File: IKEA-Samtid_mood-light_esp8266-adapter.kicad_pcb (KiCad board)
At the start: 2 copper layers, 17.5 x 17.8 mm, 11 parts, among them P1 ESP8266-01, P2 mood-light, U1 AMS1117-3.3

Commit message: ESP8266 adapter: added a bit of copper pour as heatsink.
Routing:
- net +3.3V: track 28.9 -> 31.1 mm
- added copper zone on B.Cu, net +3.3V
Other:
- board text added: "2015 - V0.30.e"
- board text removed: "2015 - V0.30.d"

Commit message: ESP8266 adapter: tweaks.
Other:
- board text added: "p.↑↓R"
- board text removed: "pull↑↓R"

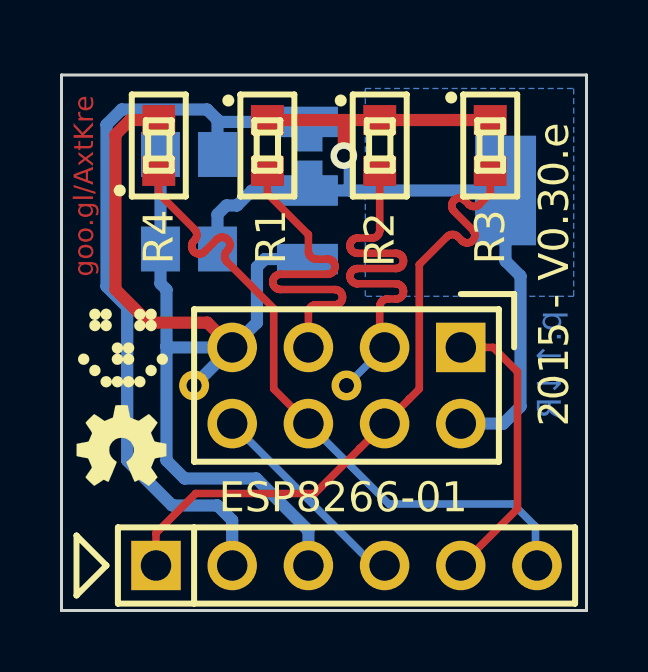
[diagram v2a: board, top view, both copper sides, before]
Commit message: ESP8266 adapter: tweaks.
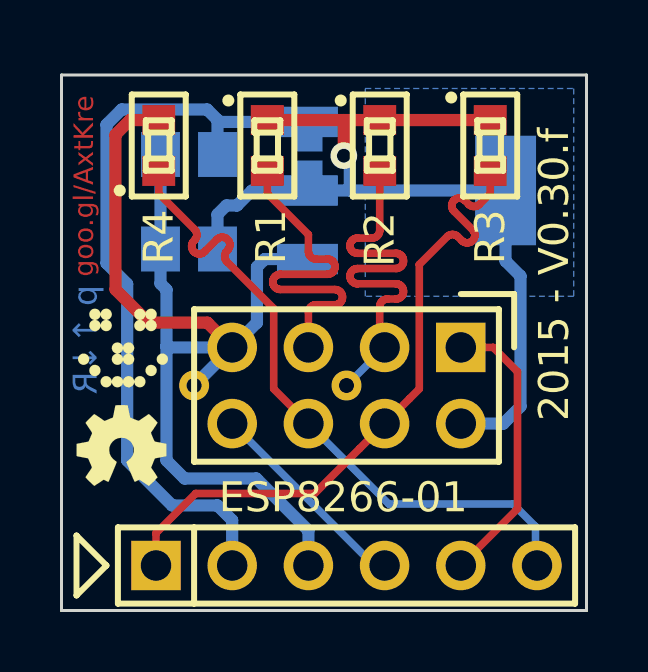
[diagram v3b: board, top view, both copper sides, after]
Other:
- board text added: "2015 - V0.30.f"
- board text removed: "2015 - V0.30.e"

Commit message: ESP8266 adapter: moved FW-UP pins to more convenient spot.
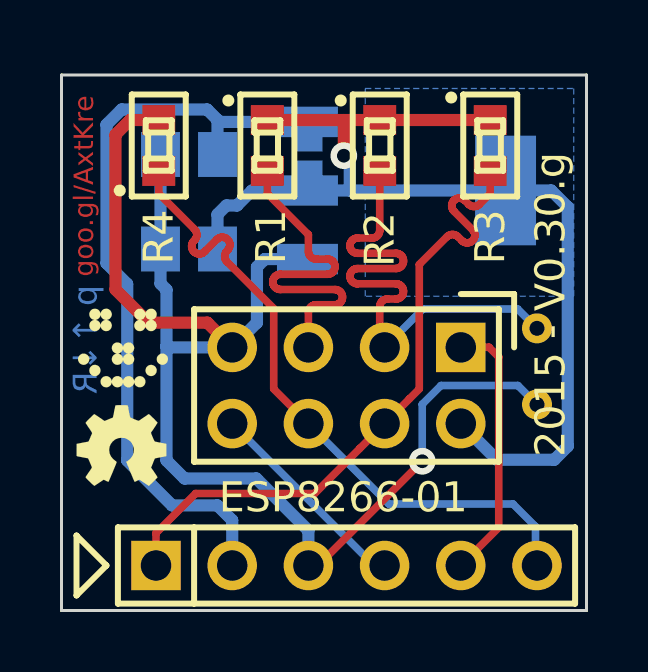
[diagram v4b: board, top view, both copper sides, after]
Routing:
- net GND: track 37.5 -> 47.2 mm, vias 0 -> 1
- net +3.3V: track 31.1 -> 36.0 mm
- net Net-(P1-Pad3): track 13.8 -> 17.9 mm
- net /RXI: track 9.47 -> 8.88 mm
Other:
- board text added: "2015 - V0.30.g"
- board text removed: "2015 - V0.30.f"
